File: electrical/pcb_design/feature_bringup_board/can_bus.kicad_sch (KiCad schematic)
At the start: 8 parts, among them J3 Molex_504050-0491, J7 Molex_504050-0491, U6 TCAN330DR

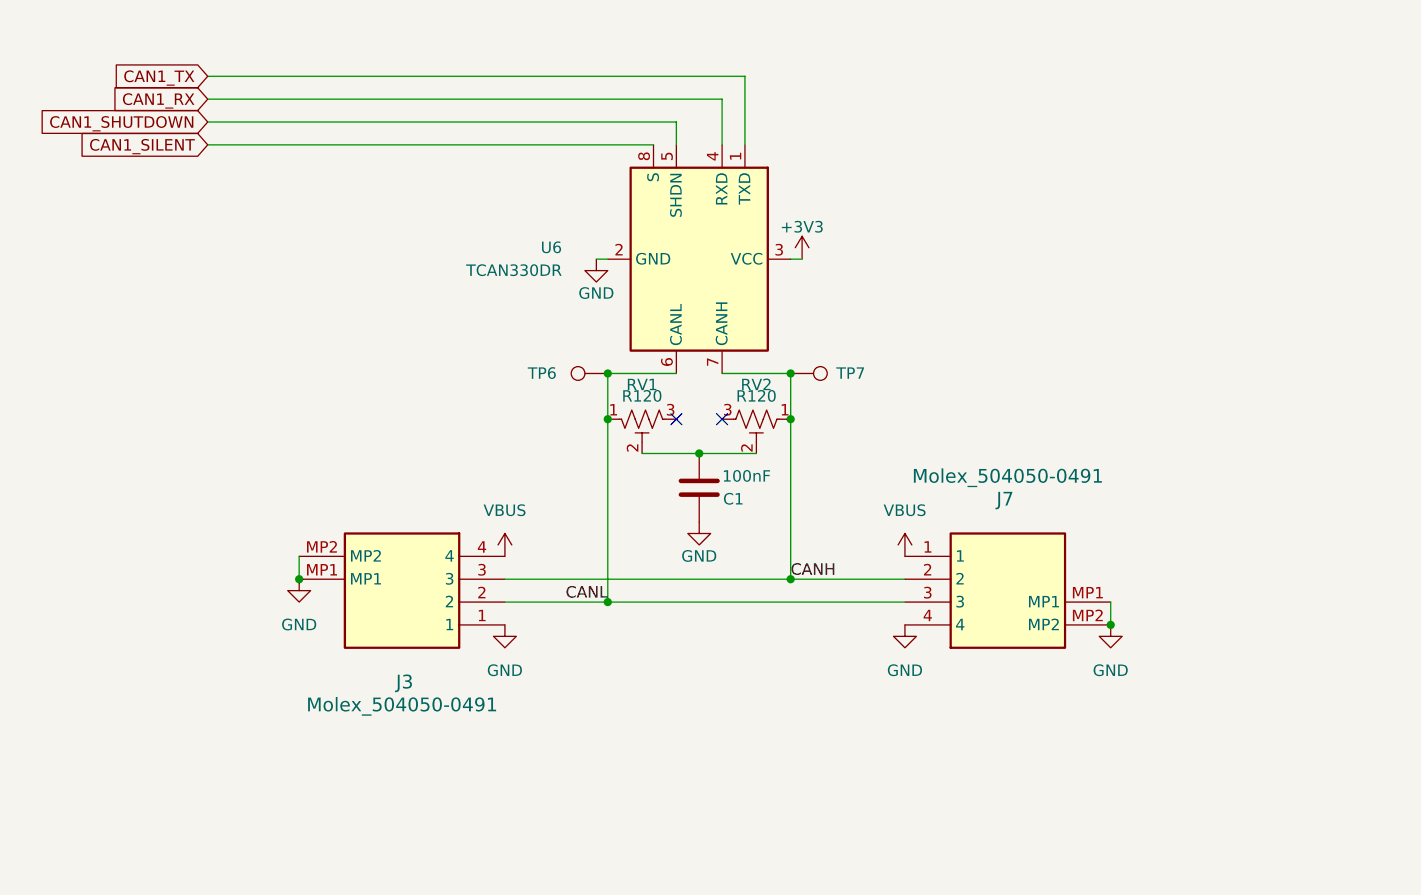
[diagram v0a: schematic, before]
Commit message: First pass on feature bringup board. All tests passing.
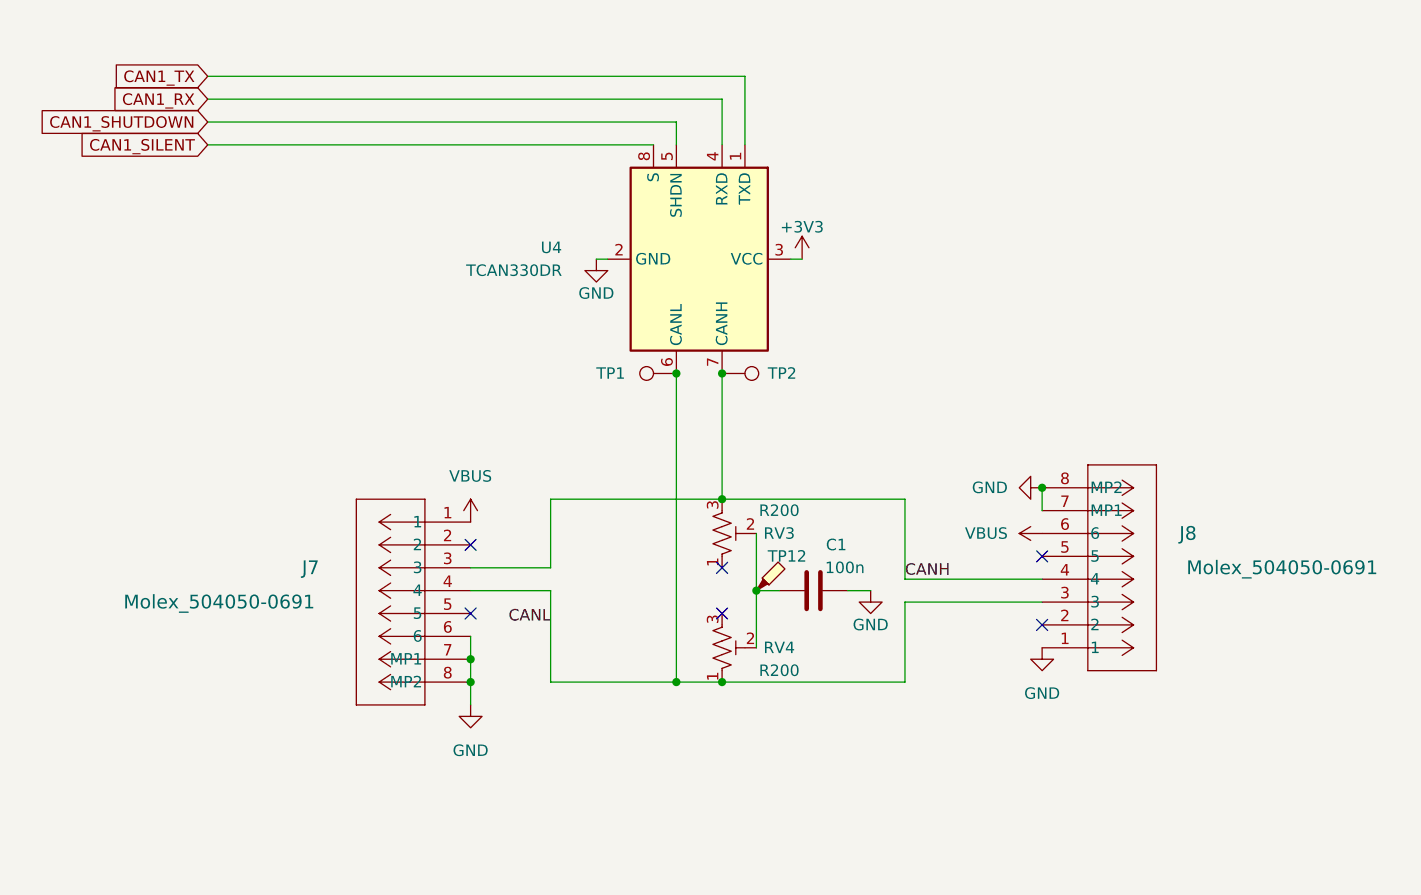
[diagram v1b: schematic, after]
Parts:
- removed J3, J7: Molex_504050-0491, footprints:Molex_504050-0491, symbol TVSC:Molex_504050-0491
- removed RV1, RV2: R120, symbol Device:R_Potentiometer_Trim_US
- added J7, J8: Molex_504050-0691, footprints:Molex_504050-0691, symbol TVSC:Molex_504050-0691
- added RV3, RV4: R200, Potentiometer_SMD:Potentiometer_Bourns_3314J_Vertical, symbol Device:R_Potentiometer_Trim_US
- added TP12: TestPoint_Probe, footprints:TestPoint_Pad_D2.5mm, symbol Connector:TestPoint_Probe
- C1: value 100nF -> 100n; footprint (none) -> footprints:Nondescript_C_0402_1005Metric
- renumbered TP6 to TP1, TP7 to TP2, U6 to U4
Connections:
- net CANH: now also J7.3, J8.4, RV3.3
- net CANL: now also J7.4, J8.3, RV4.1
- net GND: now also C1.1, J7.6, J7.7 (MP1), J7.8 (MP2), J8.1, J8.7 (MP1), J8.8 (MP2); no longer C1.2
- net VBUS: now also J7.1, J8.6
- new net: C1.2, RV3.2, RV4.2, TP12.1
- no-connect marks 2 -> 6
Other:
- moved on the sheet: TP1, TP2

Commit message: Swapped symbol/footprint/model of TCAN330 with up-to-date versions that include a 3D model.
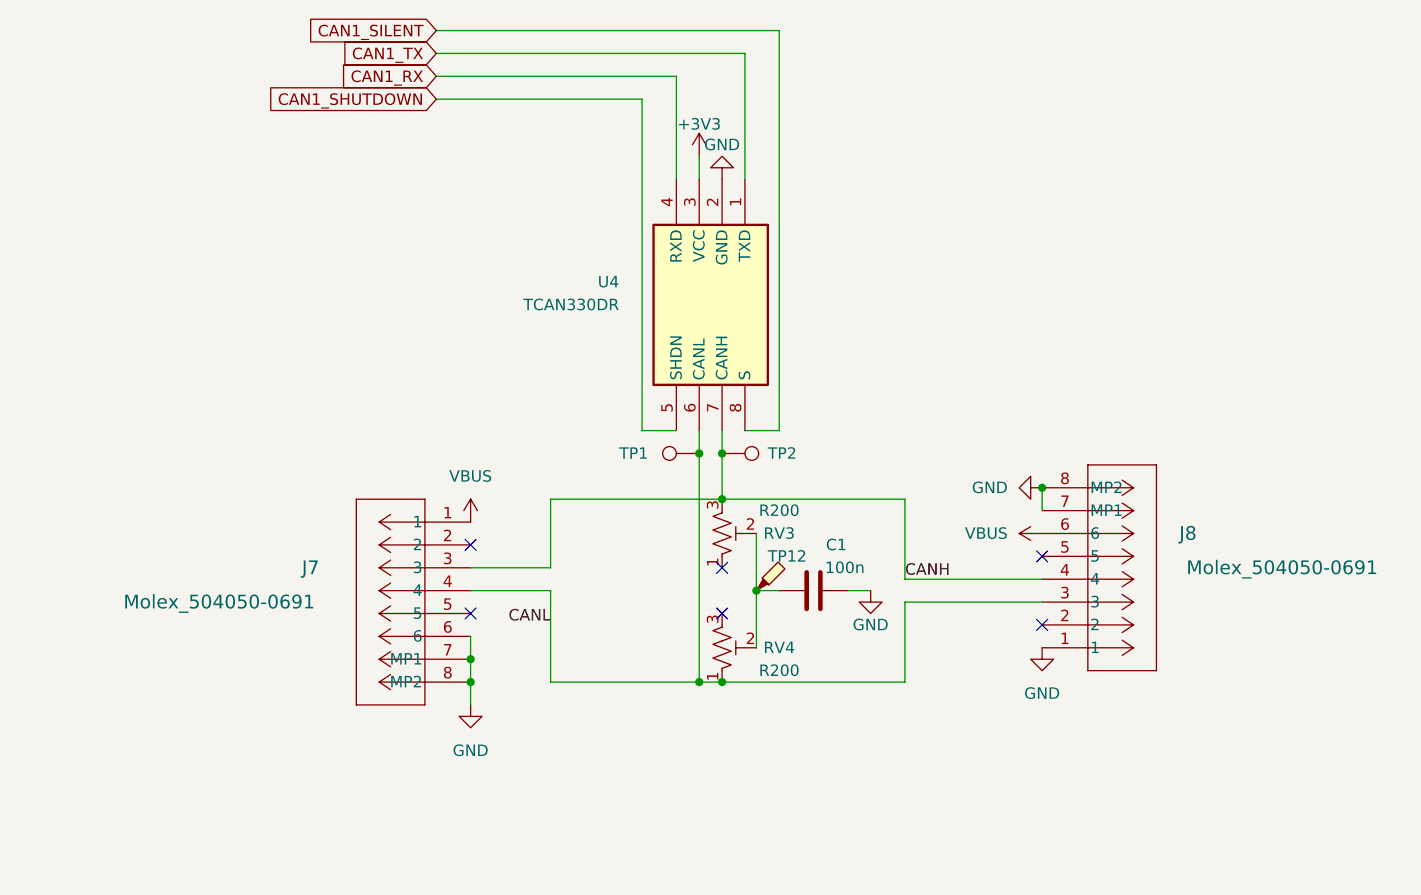
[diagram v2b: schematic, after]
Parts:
- U4: footprint Package_SO:SOIC-8-1EP_3.9x4.9mm_P1.27mm_EP2.41x3.3mm_ThermalVias -> footprints:SOIC127P600X175-8N; symbol Interface_CAN_LIN:TCAN330 -> TVSC:TCAN330DR; Arrow Part Number (none) -> TCAN330DR; Arrow Price/Stock (none) -> https://www.arrow.com/en/products/tcan330dr/texas-instrumen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; Height (none) -> 1.75; Manufacturer_Name (none) -> Texas Instruments; Manufacturer_Part_Number (none) -> TCAN330DR; Mouser Part Number (none) -> 595-TCAN330DR; Mouser Price/Stock (none) -> https://www.mouser.co.uk/ProductDetail/Texas-Instruments/TC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
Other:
- moved on the sheet: TP1, TP2, U4

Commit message: Audited MPN on parts. Marked several as NA (Not Applicable) since they do not involve any parts, but are constructs on the PCB itself.
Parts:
- TP12: MPN (none) -> NA
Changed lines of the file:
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@@
+      (effects (font (size 1.27 1.27)) hide)
+    )
+    (property "MPN" "NA" (at 163.83 111.76 0)
       (effects (font (size 1.27 1.27)) hide)
     )

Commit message: Misc tweaks and fixes, including adding bypass capacitors on power monitors, finalizing most part selections, and tweaking track layouts.
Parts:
- C1: Active (none) -> Y; MPN (none) -> C77014; Manufacturer (none) -> Murata Electronics; Manufacturer Part Number (none) -> GRM155R71E104KE14D
- TP12: Active (none) -> Y
- U4: Active (none) -> Y; Manufacturer_Name Texas Instruments -> (none); Manufacturer_Part_Number TCAN330DR -> (none)
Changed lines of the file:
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@@
+      (effects (font (size 1.27 1.27)) hide)
+    )
+    (property "Active" "Y" (at 170.18 111.76 0)
+      (effects (font (size 1.27 1.27)) hide)
+    )
+    (property "MPN" "C77014" (at 170.18 111.76 0)
+      (effects (font (size 1.27 1.27)) hide)
+    )
+    (property "Manufacturer" "Murata Electronics" (at 170.18 111.76 0)
+      (effects (font (size 1.27 1.27)) hide)
+    )
+    (property "Manufacturer Part Number" "GRM155R71E104KE14D" (at 170.18 111.76 0)
       (effects (font (size 1.27 1.27)) hide)
     )
@@
     )
     (property "MPN" "NA" (at 163.83 111.76 0)
+      (effects (font (size 1.27 1.27)) hide)
+    )
+    (property "Active" "Y" (at 163.83 111.76 0)
       (effects (font (size 1.27 1.27)) hide)
     )
@@
       (effects (font (size 1.27 1.27)) (justify left top) hide)
     )
-    (property "Manufacturer_Name" "Texas Instruments" (at -332.36 90.17 0)
-      (effects (font (size 1.27 1.27)) (justify left top) hide)
-    )
-    (property "Manufacturer_Part_Number" "TCAN330DR" (at -432.36 90.17 0)
+    (property "Manufacturer" "Texas Instruments" (at -332.36 90.17 0)
+      (effects (font (size 1.27 1.27)) (justify left top) hide)
+    )
+    (property "Manufacturer Part Number" "TCAN330DR" (at -432.36 90.17 0)
       (effects (font (size 1.27 1.27)) (justify left top) hide)
     )
@@
       (effects (font (size 1.27 1.27)) (justify left top) hide)
     )
+    (property "Active" "Y" (at 162.56 66.04 0)
+      (effects (font (size 1.27 1.27)) hide)
+    )
     (pin "2")

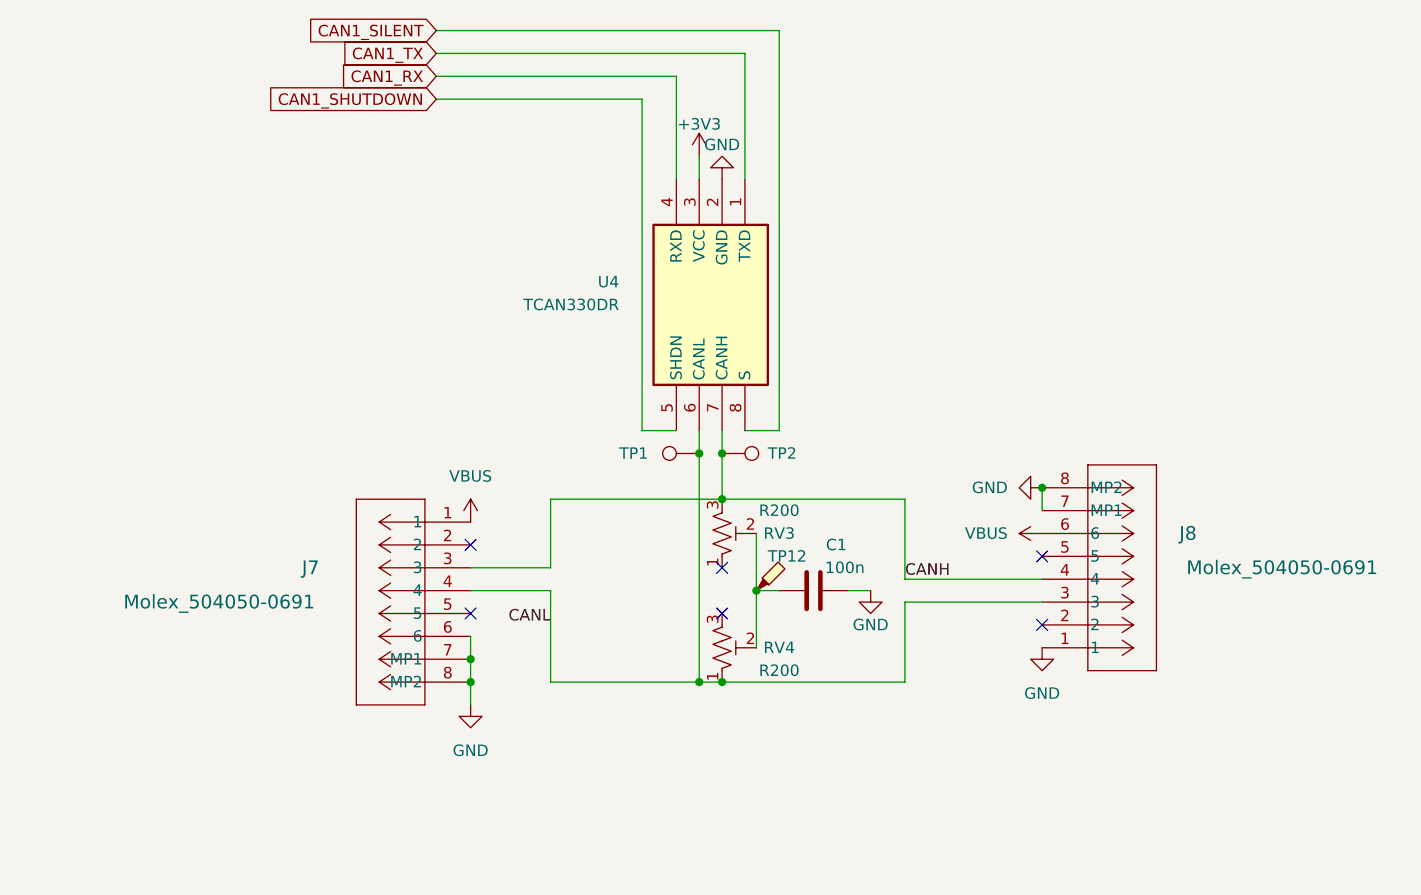
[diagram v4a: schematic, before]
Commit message: Incorporate feedback on schematic layout
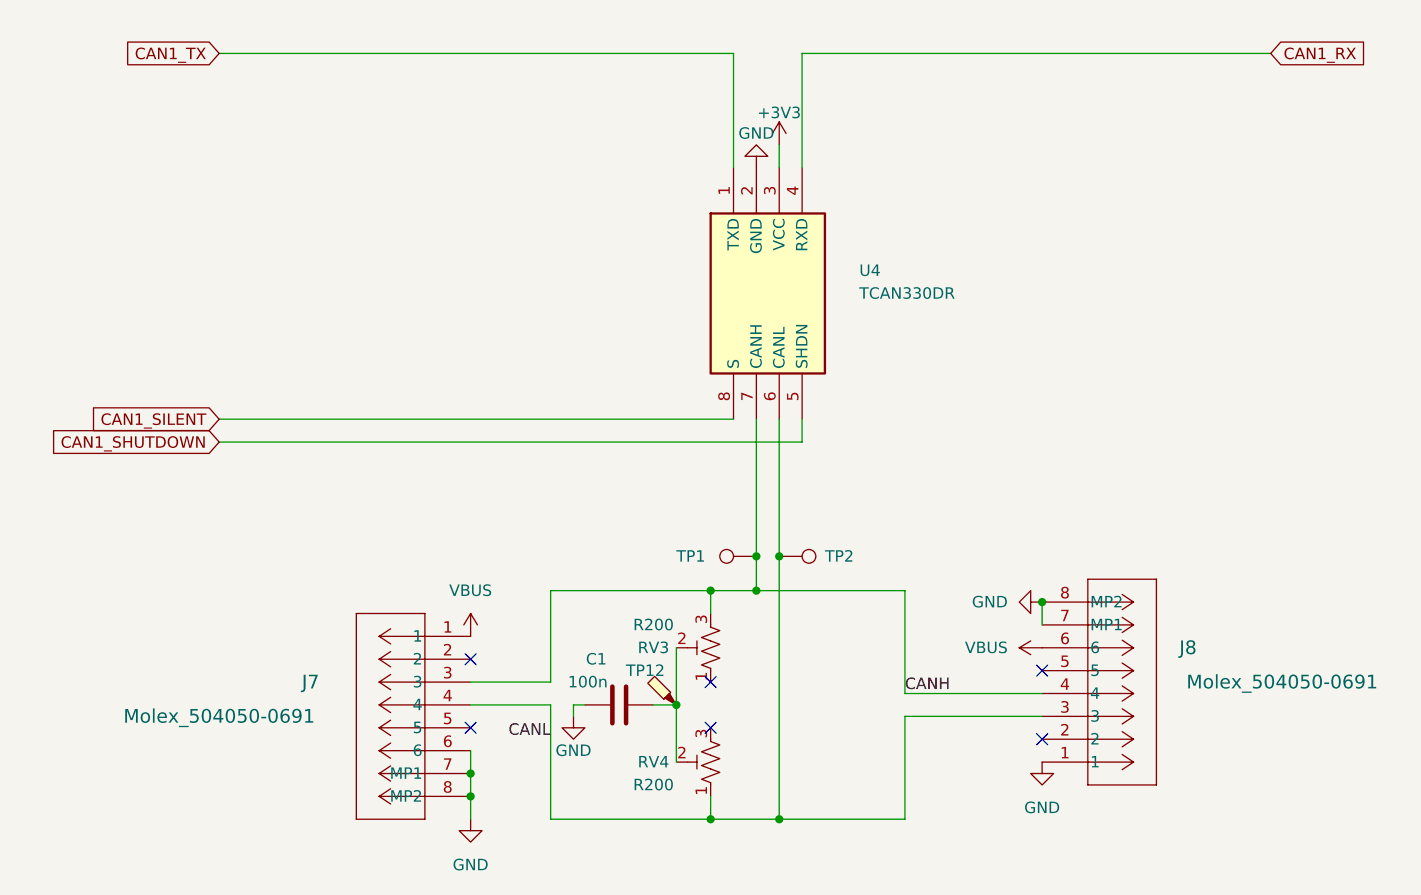
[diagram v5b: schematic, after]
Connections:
- net CANH: now also TP1.1; no longer TP2.1
- net CANL: now also TP2.1; no longer TP1.1
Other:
- moved on the sheet: C1, J7, J8, RV3, RV4, TP1, TP12, TP2
